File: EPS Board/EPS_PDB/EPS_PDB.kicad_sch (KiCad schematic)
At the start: 17 parts, among them J1 USB_B_Micro, J2 Conn_02x26_Odd_Even, J3 Conn_02x26_Odd_Even, J4 Conn_01x04_Pin, U1 AMS1117-3.3

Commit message: Started EPS PDB PCB Layout
Modified footprint of PC104 Bus
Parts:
- J4: footprint Connector_PinHeader_2.54mm:PinHeader_1x04_P2.54mm_Horizontal -> Connector_PinHeader_2.54mm:PinHeader_1x04_P2.54mm_Vertical
- JP1, JP2: footprint Connector_PinHeader_2.54mm:PinHeader_1x01_P2.54mm_Vertical -> Connector_PinHeader_2.54mm:PinHeader_1x02_P2.54mm_Vertical
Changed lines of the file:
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@@
 			)
 		)
-		(property "Footprint" "Connector_PinHeader_2.54mm:PinHeader_1x01_P2.54mm_Vertical"
+		(property "Footprint" "Connector_PinHeader_2.54mm:PinHeader_1x02_P2.54mm_Vertical"
 			(at 371.475 205.74 0)
 			(effects
@@
 			)
 		)
-		(property "Footprint" "Connector_PinHeader_2.54mm:PinHeader_1x04_P2.54mm_Horizontal"
+		(property "Footprint" "Connector_PinHeader_2.54mm:PinHeader_1x04_P2.54mm_Vertical"
 			(at 226.06 148.59 0)
 			(effects
@@
 			)
 		)
-		(property "Footprint" "Connector_PinHeader_2.54mm:PinHeader_1x01_P2.54mm_Vertical"
+		(property "Footprint" "Connector_PinHeader_2.54mm:PinHeader_1x02_P2.54mm_Vertical"
 			(at 227.965 205.74 0)
 			(effects

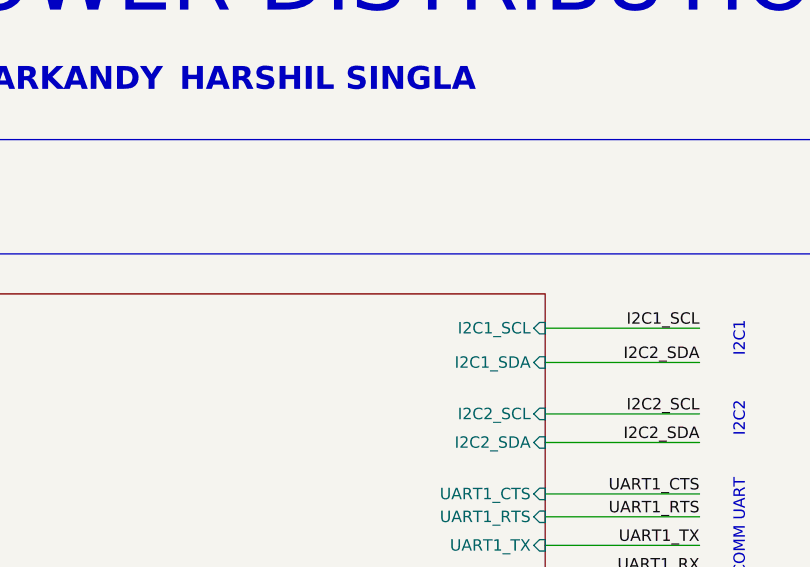
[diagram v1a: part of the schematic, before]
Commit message: PDB PCB Design Progress
Board outline copy pasted from Antenna Deployment Board
Added current limiter datasheet
Routed USB differential pair
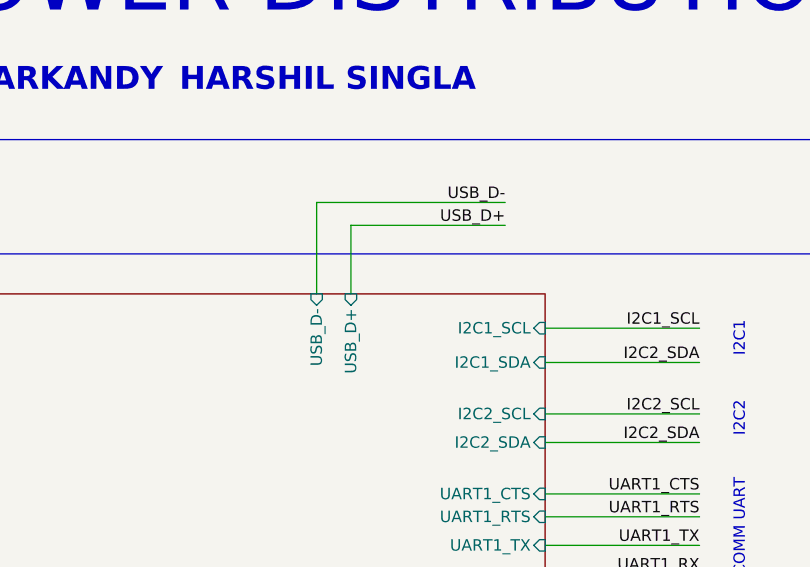
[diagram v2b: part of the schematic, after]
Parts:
- J1: footprint Connector_USB:USB_Micro-AB_Molex_47590-0001 -> Connector_USB:USB_Micro-B_GCT_USB3076-30-A
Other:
- sheet EPS Control Unit ports: added USB_D+, USB_D-; removed none
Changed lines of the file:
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@@
 	(wire
 		(pts
+			(xy 114.3 59.055) (xy 114.3 51.435)
+		)
+		(stroke
+			(width 0)
+			(type default)
+		)
+	)
+	(wire
+		(pts
 			(xy 301.625 207.01) (xy 288.29 207.01)
 		)
@@
 	(wire
 		(pts
+			(xy 114.3 51.435) (xy 131.445 51.435)
+		)
+		(stroke
+			(width 0)
+			(type default)
+		)
+	)
+	(wire
+		(pts
 			(xy 364.49 149.86) (xy 375.92 149.86)
 		)
@@
 	(wire
 		(pts
+			(xy 110.49 48.895) (xy 131.445 48.895)
+		)
+		(stroke
+			(width 0)
+			(type default)
+		)
+	)
+	(wire
+		(pts
 			(xy 242.57 205.74) (xy 247.65 205.74)
 		)
@@
 	(wire
 		(pts
+			(xy 110.49 59.055) (xy 110.49 48.895)
+		)
+		(stroke
+			(width 0)
+			(type default)
+		)
+	)
+	(wire
+		(pts
 			(xy 376.555 160.02) (xy 364.49 160.02)
 		)
@@
 		)
 	)
+	(label "USB_D-"
+		(at 131.445 48.895 180)
+		(fields_autoplaced yes)
+		(effects
+			(font
+				(size 1.27 1.27)
+			)
+			(justify right bottom)
+		)
+	)
 	(label "5V_ADCS"
 		(at 161.29 203.2 180)
@@
 		)
 	)
+	(label "USB_D+"
+		(at 131.445 51.435 180)
+		(fields_autoplaced yes)
+		(effects
+			(font
+				(size 1.27 1.27)
+			)
+			(justify right bottom)
+		)
+	)
 	(label "GND"
 		(at 371.475 121.92 0)
@@
 			)
 		)
-		(property "Footprint" "Connector_USB:USB_Micro-AB_Molex_47590-0001"
+		(property "Footprint" "Connector_USB:USB_Micro-B_GCT_USB3076-30-A"
 			(at 220.345 114.3 0)
 			(effects
@@
 			(effects
 				(font
+					(size 1.27 1.27)
+				)
+				(justify right)
+			)
+		)
+		(pin "USB_D-" input
+			(at 110.49 59.055 90)
+			(effects
+				(font
+					(size 1.27 1.27)
+				)
+				(justify right)
+			)
+		)
+		(pin "USB_D+" input
+			(at 114.3 59.055 90)
+			(effects
+				(font

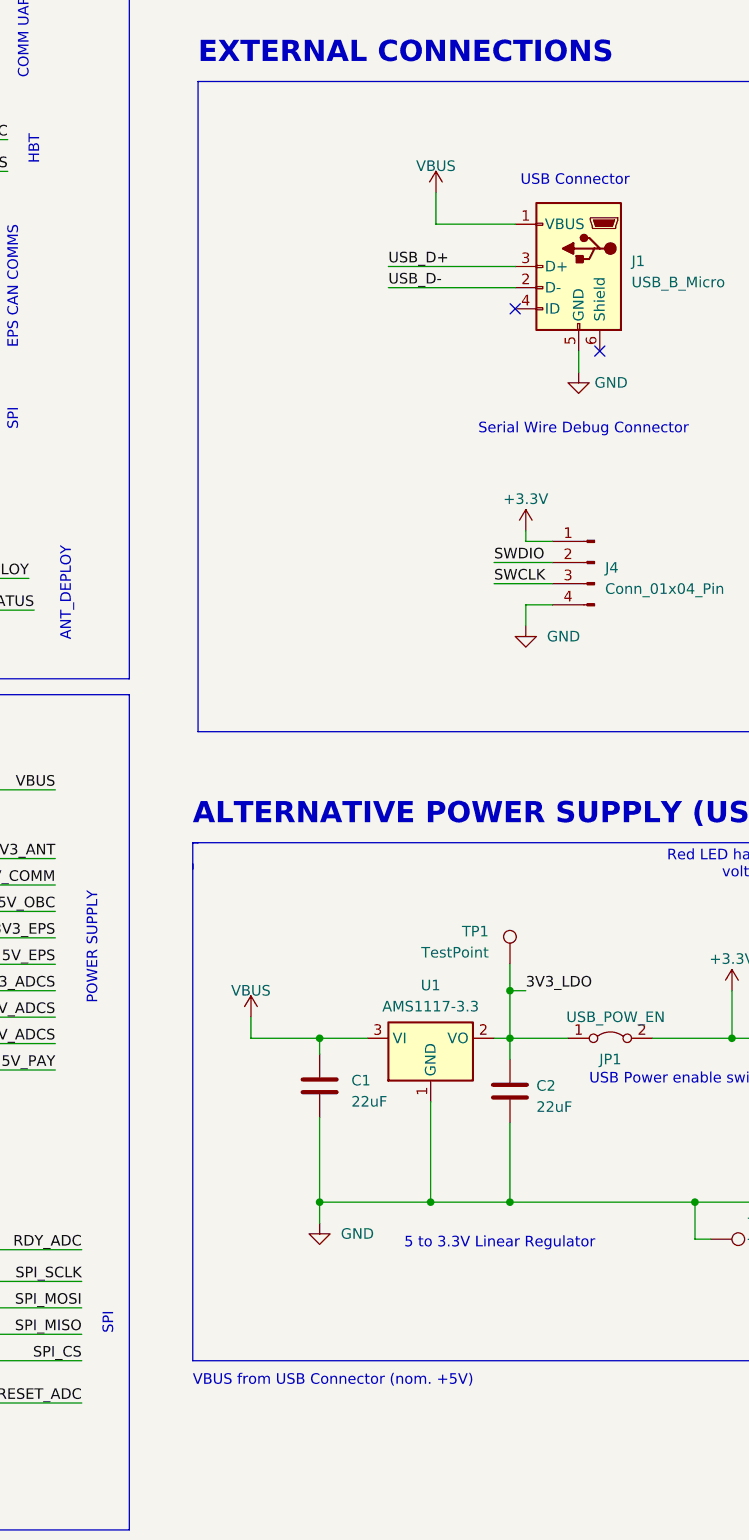
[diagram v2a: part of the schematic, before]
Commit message: Corrected mistake in USB+LDO circuit on schematic
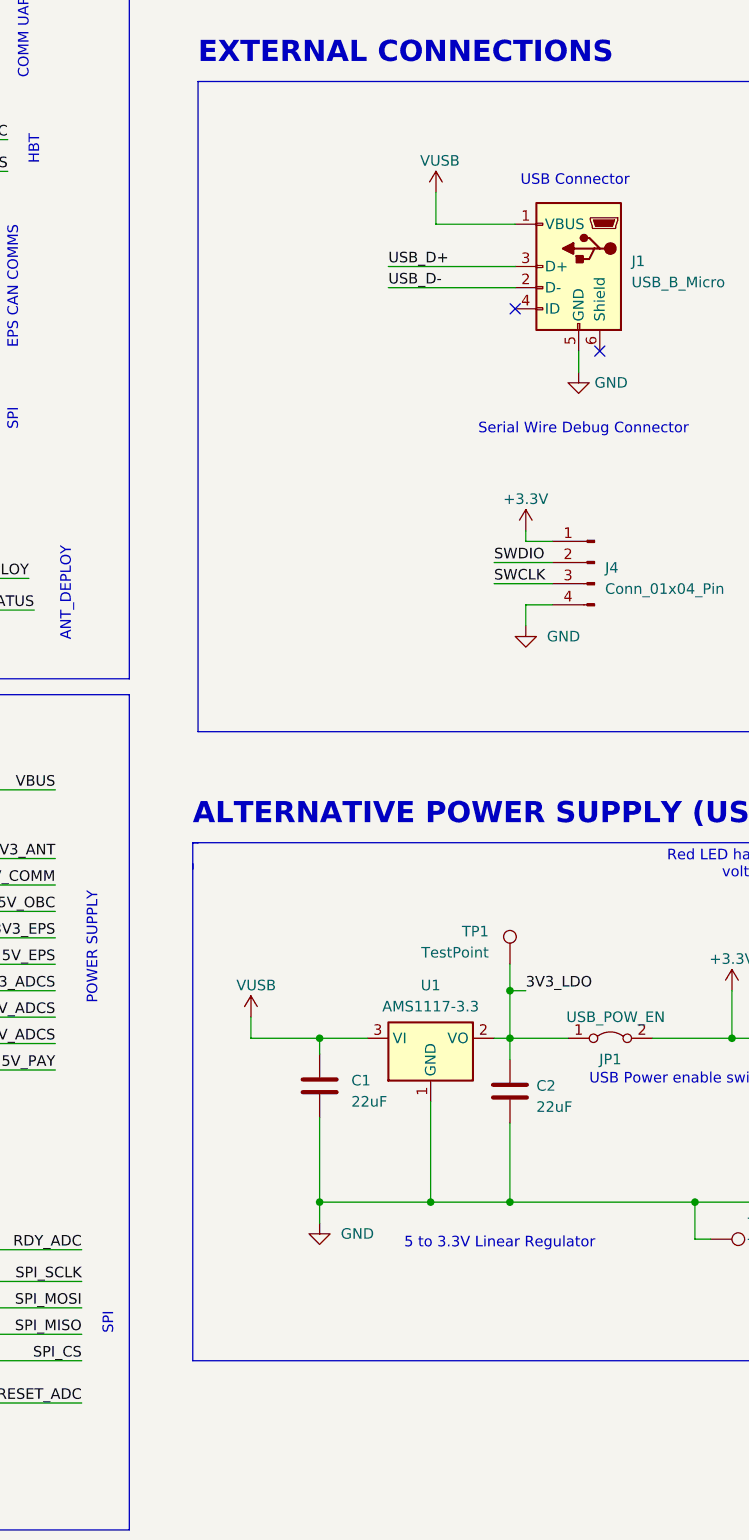
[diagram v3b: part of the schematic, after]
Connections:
- net VBUS: no longer C1.1, J1.1 (VBUS), U1.3 (VI)
- new net VUSB: C1.1, J1.1 (VBUS), U1.3 (VI)
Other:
- note removed: "VBUS from USB Connector (nom. +5V)"
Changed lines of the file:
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@@
-		)
-	)
-	(text "VBUS from USB Connector (nom. +5V)"
-		(exclude_from_sim no)
-		(at 177.8 247.65 0)
-		(effects
-			(font
-				(size 1.27 1.27)
-			)
-			(justify left bottom)
 		)
 	)
@@
 		(on_board yes)
 		(dnp no)
-		(fields_autoplaced yes)
 		(property "Reference" "#PWR02"
 			(at 207.01 107.95 0)
@@
 			)
 		)
-		(property "Value" "VBUS"
-			(at 207.01 100.965 0)
-			(effects
-				(font
-					(size 1.27 1.27)
-				)
+		(property "Value" "VUSB"
+			(at 205.105 100.33 0)
+			(effects
+				(font
+					(size 1.27 1.27)
+				)
+				(justify left)
 			)
 		)
@@
 		(on_board yes)
 		(dnp no)
-		(fields_autoplaced yes)
 		(property "Reference" "#PWR09"
 			(at 184.785 207.01 0)
@@
 			)
 		)
-		(property "Value" "VBUS"
-			(at 184.785 200.025 0)
-			(effects
-				(font
+		(property "Value" "VUSB"
+			(at 185.42 199.39 0)
+			(effects
+				(font

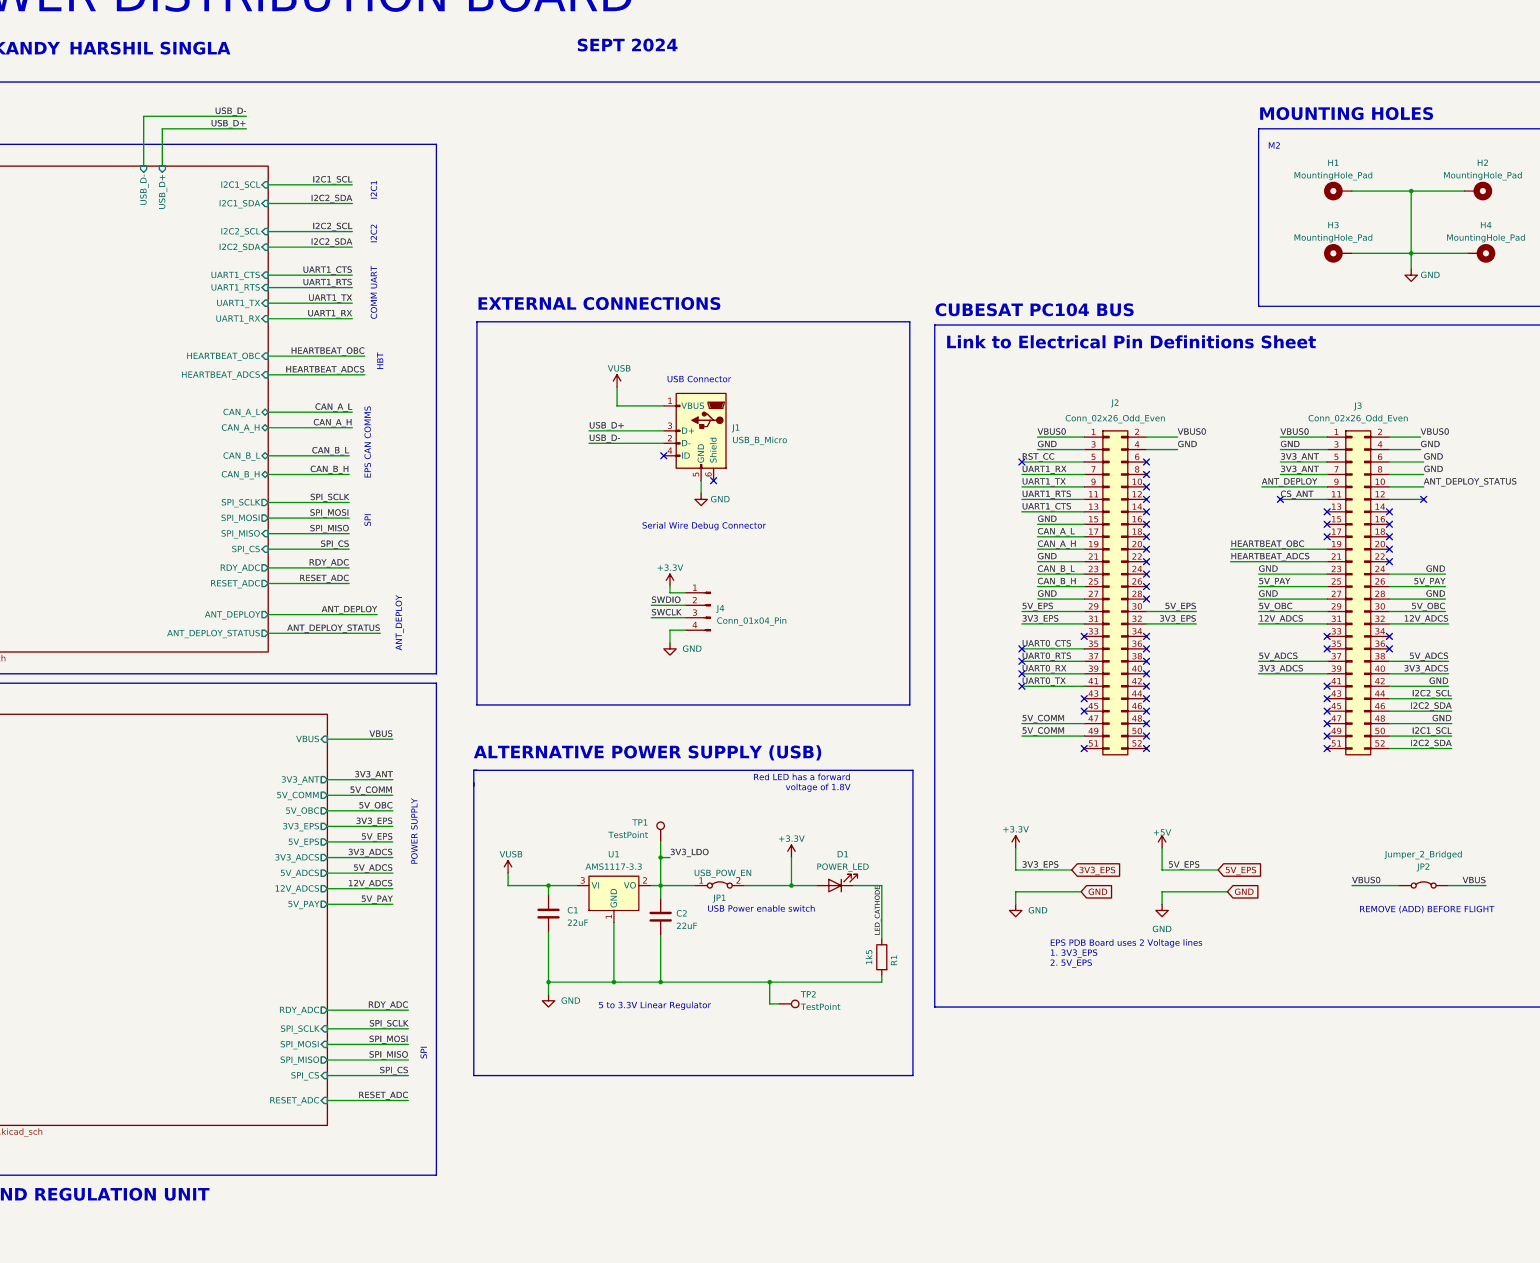
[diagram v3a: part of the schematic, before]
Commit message: EPS PDB Board Layout Progress
Fixed issue with outline,
added correct outline
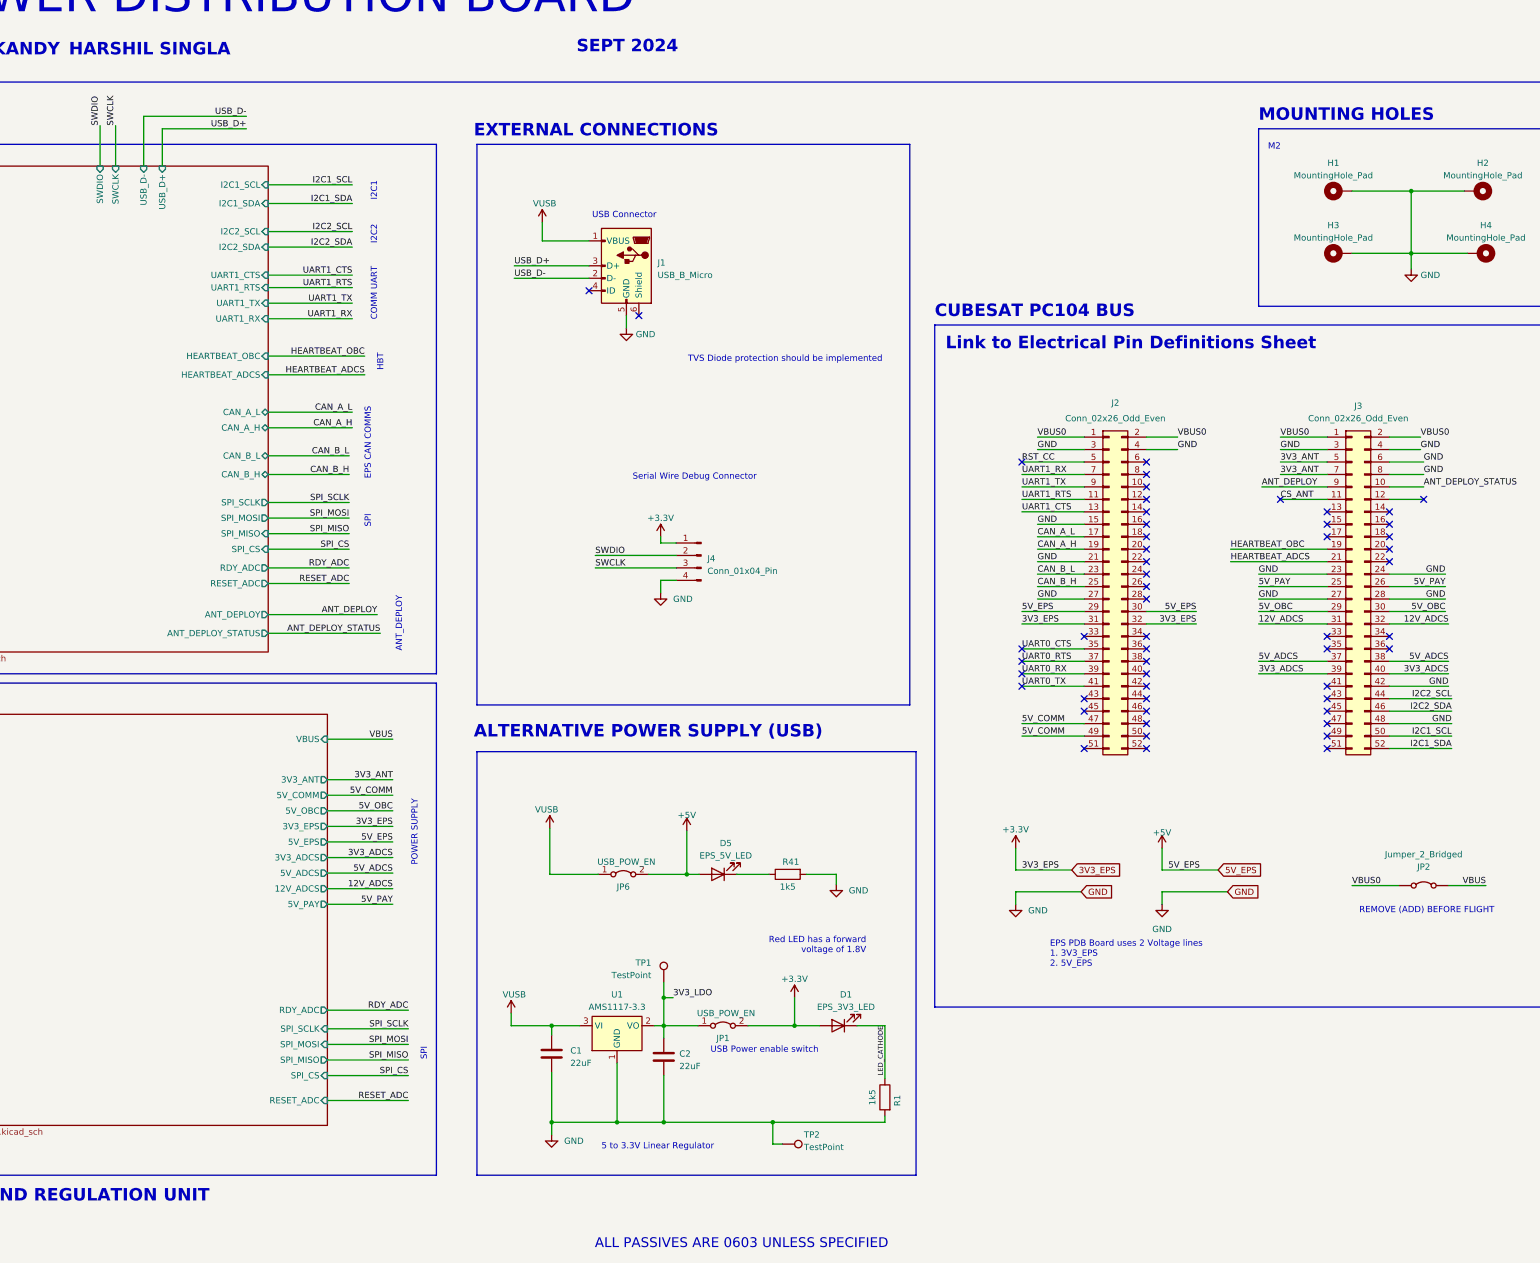
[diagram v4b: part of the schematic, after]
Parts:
- added D5: EPS_5V_LED, LED_SMD:LED_0805_2012Metric, symbol Device:LED
- added JP6: USB_POW_EN, Connector_PinHeader_2.54mm:PinHeader_1x02_P2.54mm_Vertical, symbol Jumper:Jumper_2_Bridged
- added R41: 1k5, Resistor_SMD:R_0603_1608Metric, symbol Device:R
- C1, C2: footprint Capacitor_SMD:C_0805_2012Metric -> Capacitor_SMD:C_0603_1608Metric
- D1: value POWER_LED -> EPS_3V3_LED
- H1, H2, H3, H4: footprint MountingHole:MountingHole_2.2mm_M2_DIN965_Pad -> MountingHole:MountingHole_3.2mm_M3_Pad
- J4: footprint Connector_PinHeader_2.54mm:PinHeader_1x04_P2.54mm_Vertical -> Connector_PinHeader_2.54mm:PinHeader_1x04_P2.54mm_Horizontal
- R1: footprint Resistor_SMD:R_0805_2012Metric -> Resistor_SMD:R_0603_1608Metric
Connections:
- net +5V: now also D5.2 (A), JP6.2 (B)
- net GND: now also R41.2
- net I2C2_SDA: no longer J3.52 (Pin_52)
- net VUSB: now also JP6.1 (A)
- new net: D5.1 (K), R41.1
- new net I2C1_SDA: J3.52 (Pin_52)
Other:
- sheet EPS Control Unit ports: added SWCLK, SWDIO; removed none
- note added: "ALL PASSIVES ARE 0603 UNLESS SPECIFIED"
- note added: "TVS Diode protection should be implemented"
- moved on the sheet: C1, C2, D1, J1, J4, JP1, R1, TP1, TP2, U1
